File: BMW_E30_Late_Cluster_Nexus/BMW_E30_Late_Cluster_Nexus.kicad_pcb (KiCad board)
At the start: 2 copper layers, 356.8 x 150 mm, 38 parts, among them J1 Blue, J2 White, J3 Yellow, J4 Speedometer, J5 SI Connector, J6 Tachometer, Q1 BC327, U1 Coolant Temp, U2 Fuel Gauge

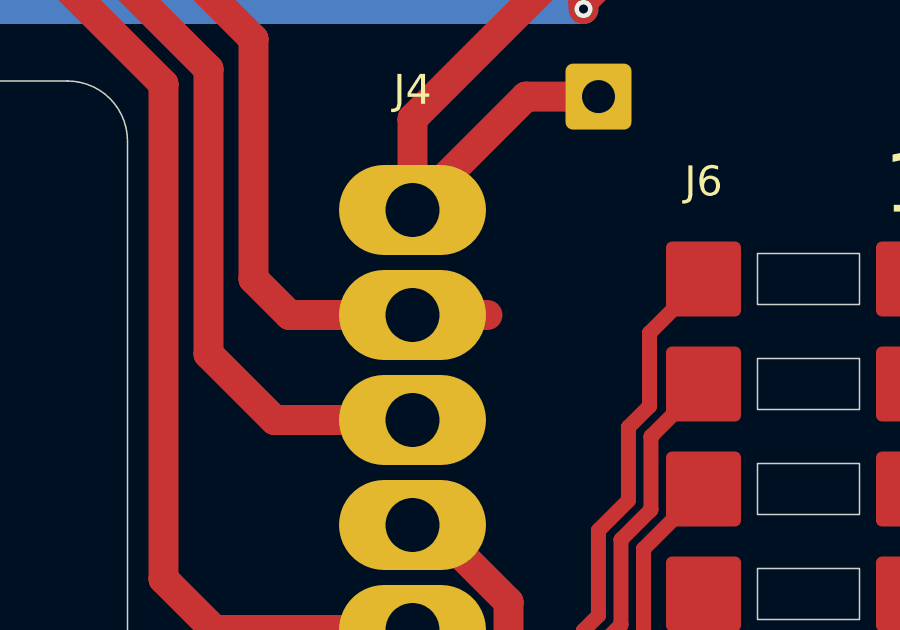
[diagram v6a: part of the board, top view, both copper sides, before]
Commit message: Updated Resistor Value
R28 Value was incorrect, changed from 200R to 200k ohms
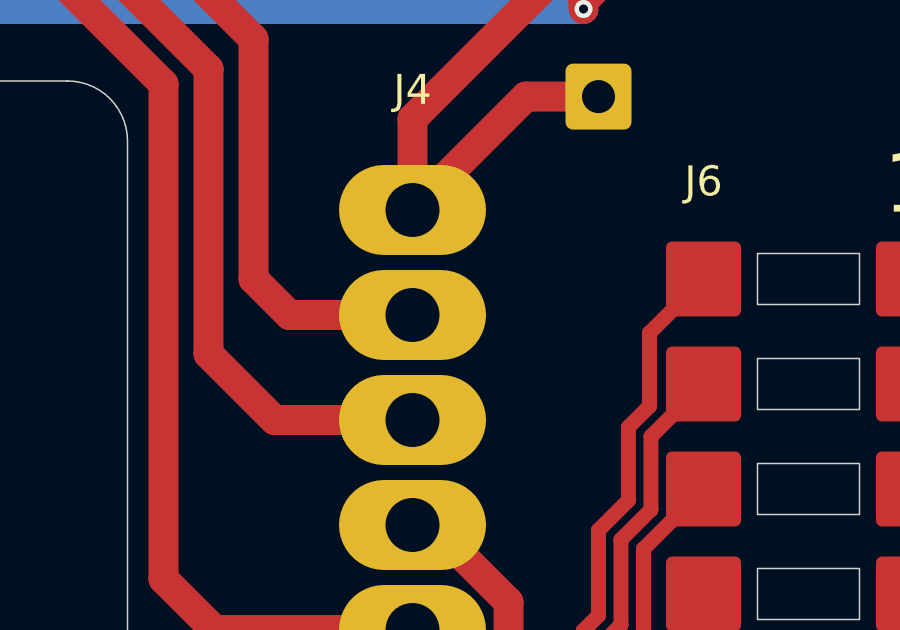
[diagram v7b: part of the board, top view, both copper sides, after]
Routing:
- net GNDPWR: track 971.9 -> 969.4 mm
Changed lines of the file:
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@@
-	)
-	(segment
-		(start 213.3 134.2)
-		(end 215.8 134.2)
-		(width 1)
-		(layer "F.Cu")
-		(net 27)
 	)
 	(segment

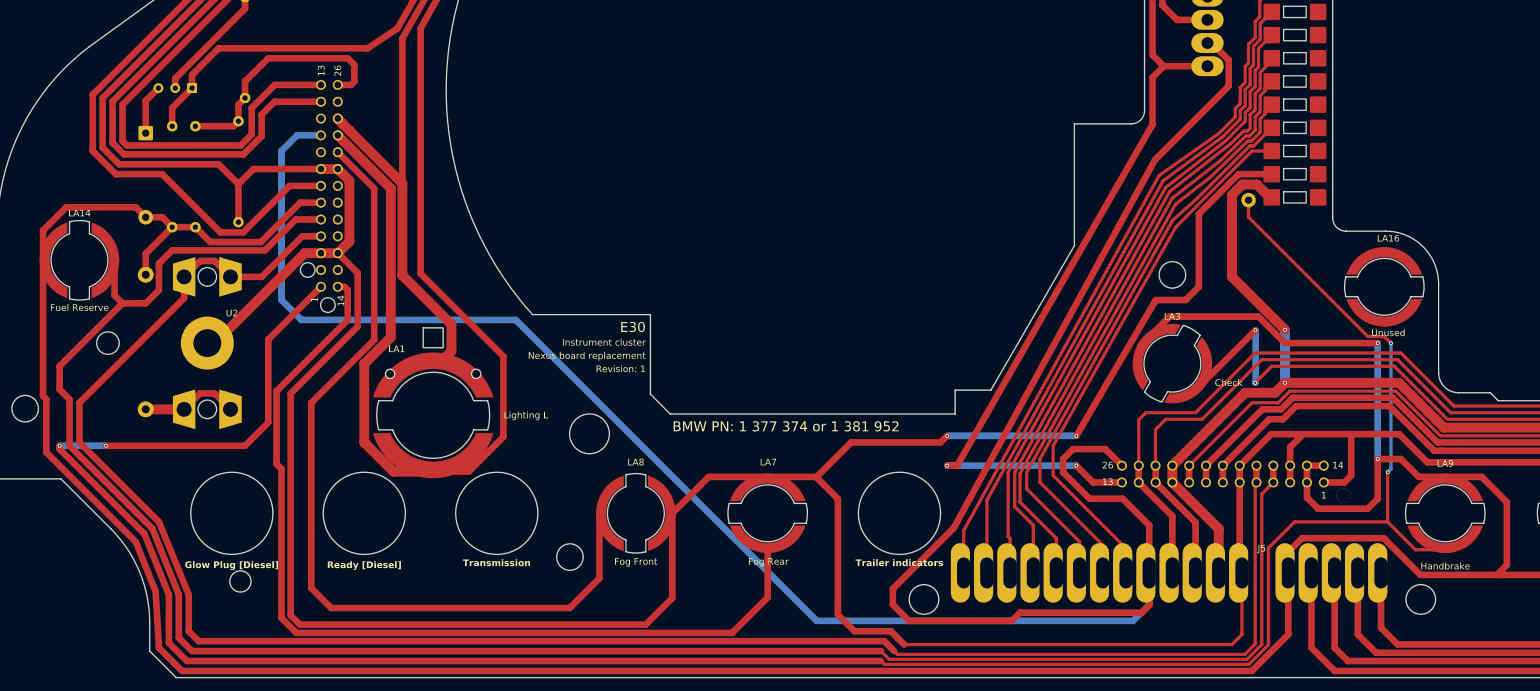
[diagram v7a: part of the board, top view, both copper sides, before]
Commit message: Update Connector V
Change Connector V to an updated version that is more accurate to the original pins. Note that depending on Early model updates and subsequent board runs, the outline may have to be moved up by 0.2 mm to match it. Also further adjustments of many connectors may need to be updated slightly for fitment purposes
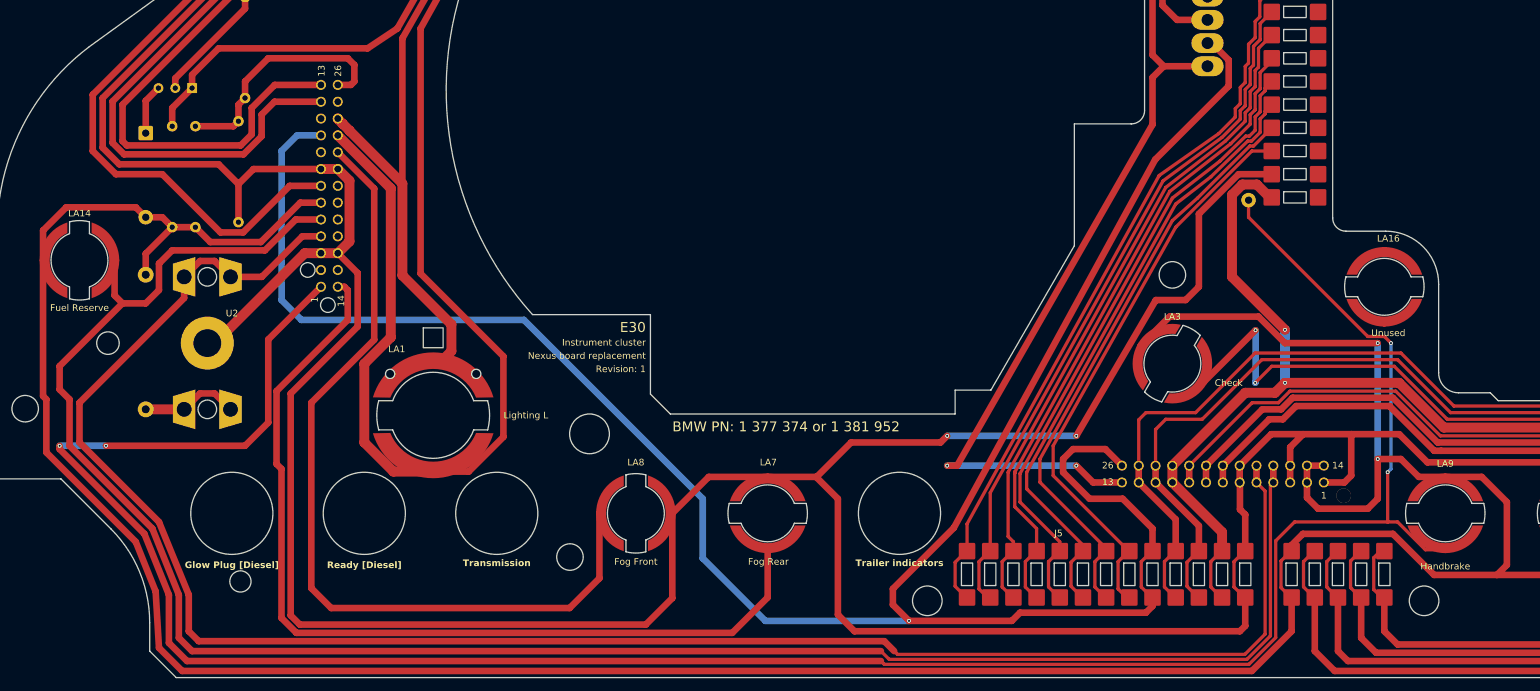
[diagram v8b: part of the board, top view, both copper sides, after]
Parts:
- J5: footprint BMW_Cluster_Connectors:ConnectorV_Late -> BMW_Cluster_Connectors:ConnectorV_Late_V2
- moved J5 0.54 mm to (240.0, 221.4)
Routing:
- net Wheel_spd_output: track 370.6 -> 336.1 mm, vias 0 -> 1
- net EG_2+: track 80.9 -> 86.5 mm
- net Engine_spd_input: track 168.5 -> 174.0 mm
- net EG_1-: track 86.6 -> 92.2 mm
- net EG_2-: track 83.0 -> 88.4 mm
- net EG_1+: track 89.5 -> 95.0 mm
- net Tach_1-: track 94.8 -> 100.2 mm
- net Fuel_rate_input: track 206.2 -> 211.6 mm
- net +12_T30: track 221.9 -> 227.3 mm
- net Tach_2+: track 99.2 -> 104.5 mm
- net Tach_2-: track 103.8 -> 109.0 mm
- net Tach_1+: track 92.3 -> 97.4 mm
- net Temp_+Ub: track 180.1 -> 185.1 mm
- net SI_RST: track 253.6 -> 258.3 mm
- net Eng_temp_sensor: track 320.0 -> 324.6 mm
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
